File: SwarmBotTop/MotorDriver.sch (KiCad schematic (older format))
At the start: 12 parts, among them U3 STSPIN220

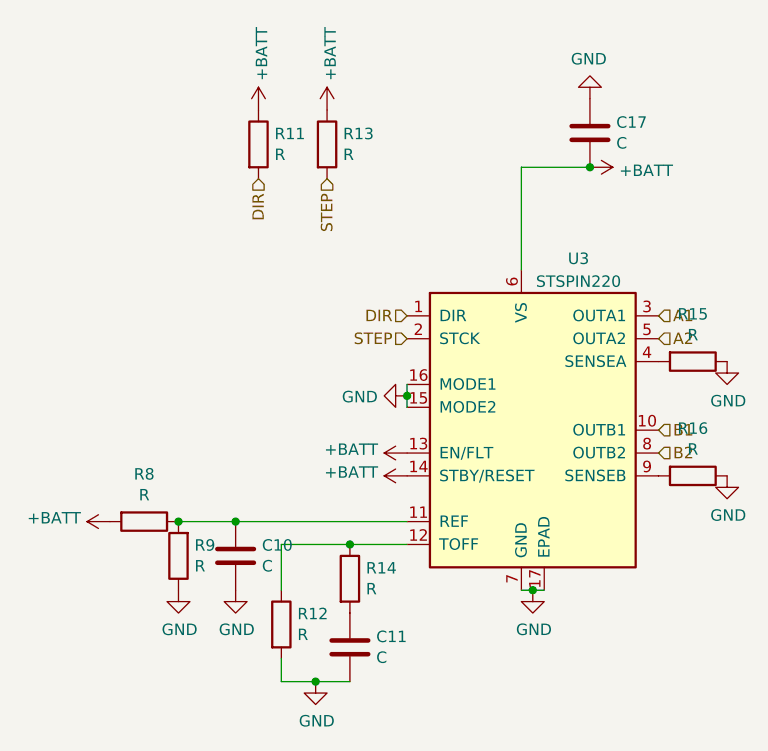
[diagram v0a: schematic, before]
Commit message: Camera routing with all sensors and motors
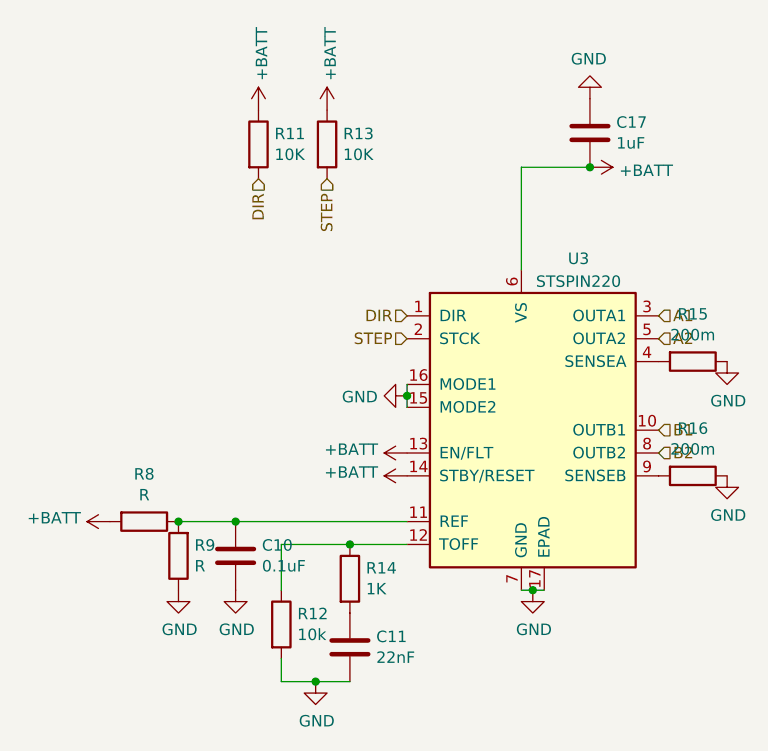
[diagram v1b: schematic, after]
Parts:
- C10: value C -> 0.1uF
- C11: value C -> 22nF
- C17: value C -> 1uF
- R11, R13: value R -> 10K
- R12: value R -> 10k
- R14: value R -> 1K
- R15, R16: value R -> 200m
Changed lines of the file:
@@
 P 3650 1700
 F 0 "R11" H 3720 1746 50  0000 L CNN
-F 1 "R" H 3720 1655 50  0000 L CNN
+F 1 "10K" H 3720 1655 50  0000 L CNN
 F 2 "Resistor_SMD:R_0402_1005Metric" V 3580 1700 50  0001 C CNN
 F 3 "~" H 3650 1700 50  0001 C CNN
@@
 P 3950 1700
 F 0 "R13" H 4020 1746 50  0000 L CNN
-F 1 "R" H 4020 1655 50  0000 L CNN
+F 1 "10K" H 4020 1655 50  0000 L CNN
 F 2 "Resistor_SMD:R_0402_1005Metric" V 3880 1700 50  0001 C CNN
 F 3 "~" H 3950 1700 50  0001 C CNN
@@
 P 4050 3600
 F 0 "R14" H 4120 3646 50  0000 L CNN
-F 1 "R" H 4120 3555 50  0000 L CNN
+F 1 "1K" H 4120 3555 50  0000 L CNN
 F 2 "Resistor_SMD:R_0402_1005Metric" V 3980 3600 50  0001 C CNN
 F 3 "~" H 4050 3600 50  0001 C CNN
@@
 P 4050 3900
 F 0 "C11" H 4165 3946 50  0000 L CNN
-F 1 "C" H 4165 3855 50  0000 L CNN
+F 1 "22nF" H 4165 3855 50  0000 L CNN
 F 2 "Capacitor_SMD:C_0402_1005Metric" H 4088 3750 50  0001 C CNN
 F 3 "~" H 4050 3900 50  0001 C CNN
@@
 P 3750 3800
 F 0 "R12" H 3820 3846 50  0000 L CNN
-F 1 "R" H 3820 3755 50  0000 L CNN
+F 1 "10k" H 3820 3755 50  0000 L CNN
 F 2 "Resistor_SMD:R_0402_1005Metric" V 3680 3800 50  0001 C CNN
 F 3 "~" H 3750 3800 50  0001 C CNN
@@
 P 3550 3500
 F 0 "C10" H 3665 3546 50  0000 L CNN
-F 1 "C" H 3665 3455 50  0000 L CNN
+F 1 "0.1uF" H 3665 3455 50  0000 L CNN
 F 2 "Capacitor_SMD:C_0402_1005Metric" H 3588 3350 50  0001 C CNN
 F 3 "~" H 3550 3500 50  0001 C CNN
@@
 P 5550 2650
 F 0 "R15" V 5343 2650 50  0000 C CNN
-F 1 "R" V 5434 2650 50  0000 C CNN
+F 1 "200m" V 5434 2650 50  0000 C CNN
 F 2 "Resistor_SMD:R_0402_1005Metric" V 5480 2650 50  0001 C CNN
 F 3 "~" H 5550 2650 50  0001 C CNN
@@
 P 5550 3150
 F 0 "R16" V 5343 3150 50  0000 C CNN
-F 1 "R" V 5434 3150 50  0000 C CNN
+F 1 "200m" V 5434 3150 50  0000 C CNN
 F 2 "Resistor_SMD:R_0402_1005Metric" V 5480 3150 50  0001 C CNN
 F 3 "~" H 5550 3150 50  0001 C CNN
@@
 P 5100 1650
 F 0 "C17" H 5215 1696 50  0000 L CNN
-F 1 "C" H 5215 1605 50  0000 L CNN
+F 1 "1uF" H 5215 1605 50  0000 L CNN
 F 2 "Capacitor_SMD:C_0402_1005Metric" H 5138 1500 50  0001 C CNN
 F 3 "~" H 5100 1650 50  0001 C CNN
